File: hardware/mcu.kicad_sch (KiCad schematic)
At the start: 25 parts, among them J6 Debug, SW1 BOOT, SW2 RESET, U3 STM32F405RGTx, Y1 8MHz

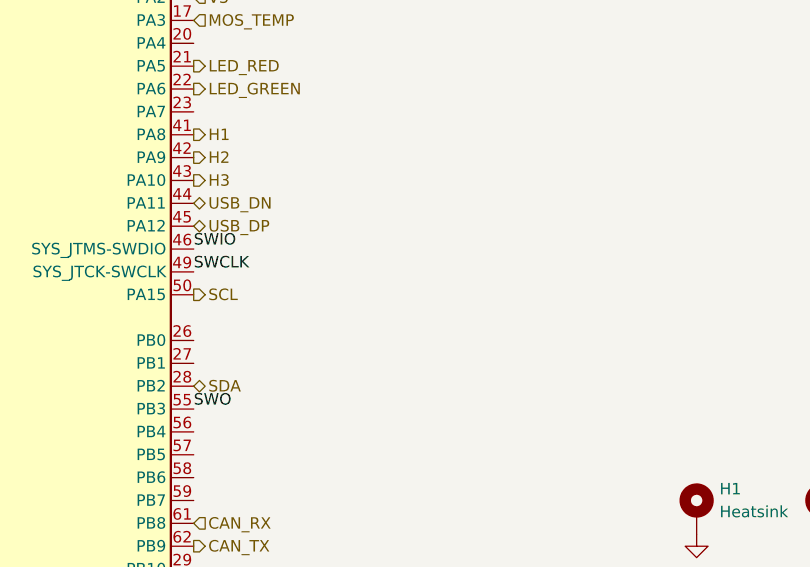
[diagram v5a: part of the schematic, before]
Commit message: Add missing I2C pullups
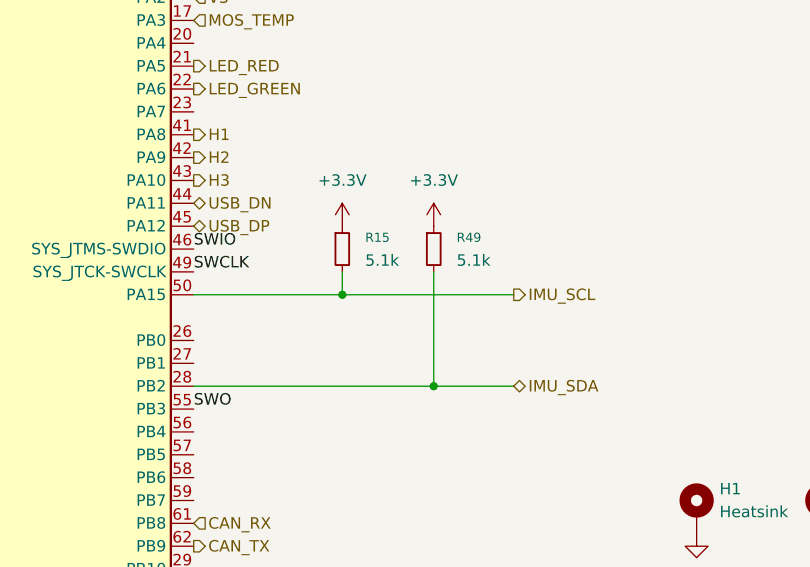
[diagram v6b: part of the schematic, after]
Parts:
- added R15, R49: 5.1k, Resistor_SMD:R_0402_1005Metric, symbol Device:R_Small
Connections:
- net +3.3V: now also R15.1, R49.1
- net SCL renamed IMU_SCL
- net IMU_SCL: now also R15.2
- net SDA renamed IMU_SDA
- net IMU_SDA: now also R49.2
